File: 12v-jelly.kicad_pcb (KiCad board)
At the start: 4 copper layers, 46 x 68 mm, 28 parts, among them J1 PWR, J10 8, J3 1, J4 2, J5 3, J6 4, J7 5, J8 6, J9 7, SW2 SW_Push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

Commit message: MOSFET
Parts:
- added Q1: Q_NMOS_GDS, Package_TO_SOT_SMD:TO-252-3_TabPin2, F.Cu at (80.2, 24.8)
- added R4: 10k, Resistor_SMD:R_0603_1608Metric, F.Cu at (90.8, 26.2)
- moved U3 5.05 mm to (80.0, 44.8)
- moved U1 4.25 mm to (80.0, 66.2)
- moved C1 4.25 mm to (86.0, 68.0)
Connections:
- C1 pad 1: +5V -> LED_PWR
- J10 pad 3: +5V -> LED_PWR
- J3 pad 3: +5V -> LED_PWR
- J4 pad 3: +5V -> LED_PWR
- J5 pad 3: +5V -> LED_PWR
- J6 pad 3: +5V -> LED_PWR
- J7 pad 3: +5V -> LED_PWR
- J8 pad 3: +5V -> LED_PWR
- J9 pad 3: +5V -> LED_PWR
- U1 pad 10: +5V -> LED_PWR
- U1 pad 16: +5V -> LED_PWR
- U2 pad 2: unconnected-(U2-GPIO1-Pad2) -> /LED_EN
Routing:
- net +5V: track 26.1 -> 83.4 mm, vias 2 -> 1
- net LED_PWR: track 0.00 -> 13.7 mm, vias 0 -> 9
- net /LED_EN: track 0.00 -> 7.15 mm, vias 0 -> 1
- net Net-(J4-Pin_2): track 32.9 -> 37.2 mm
- net Net-(J10-Pin_2): track 40.9 -> 45.2 mm
- net Net-(J9-Pin_2): track 31.8 -> 36.1 mm
- net Net-(J8-Pin_2): track 32.5 -> 36.8 mm
- net Net-(J6-Pin_2): track 43.6 -> 47.9 mm
- net Net-(J5-Pin_2): track 33.5 -> 37.7 mm
- net Net-(J7-Pin_2): track 43.3 -> 47.6 mm
- net Net-(J3-Pin_2): track 47.6 -> 51.9 mm
- net /CLOCK: track 11.8 -> 9.67 mm
- net /DATA: track 26.3 -> 28.1 mm
- net /LATCH: track 11.3 -> 13.0 mm
- net Net-(J1-Pin_2): track 22.9 -> 21.2 mm
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- added copper zone on F.Cu, net +5V
- added copper zone on F.Cu, net LED_PWR
- added copper zone on In1.Cu, net LED_PWR
- removed copper zone on In1.Cu, net +5V
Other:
- board text added: "12v Jelly Eve Bytheway 24-04-01"

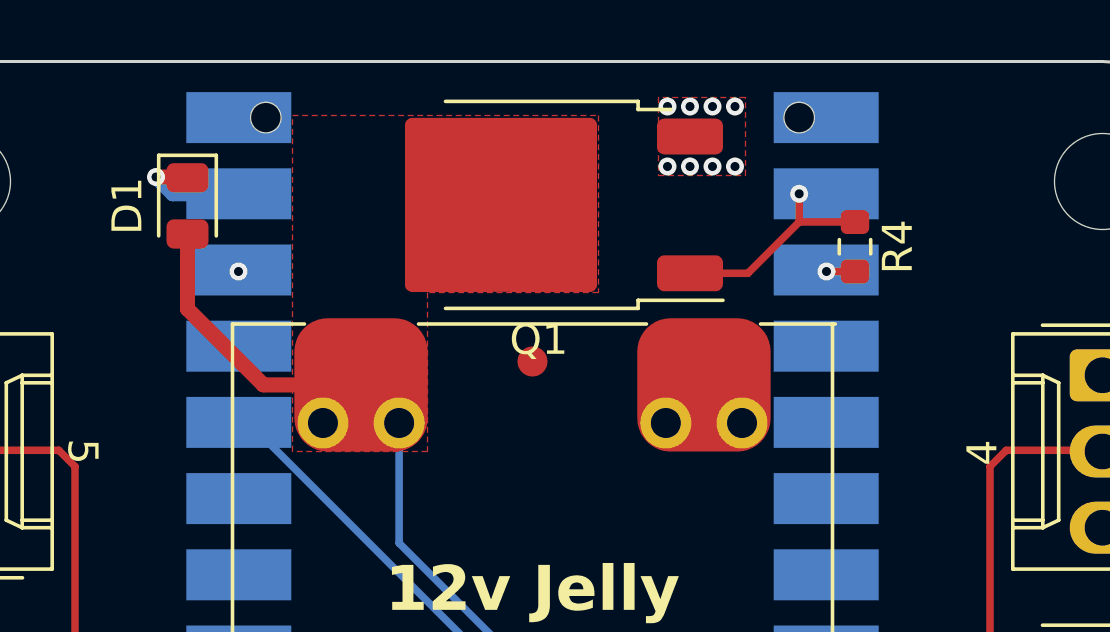
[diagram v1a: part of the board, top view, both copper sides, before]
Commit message: PMOS not NMOS
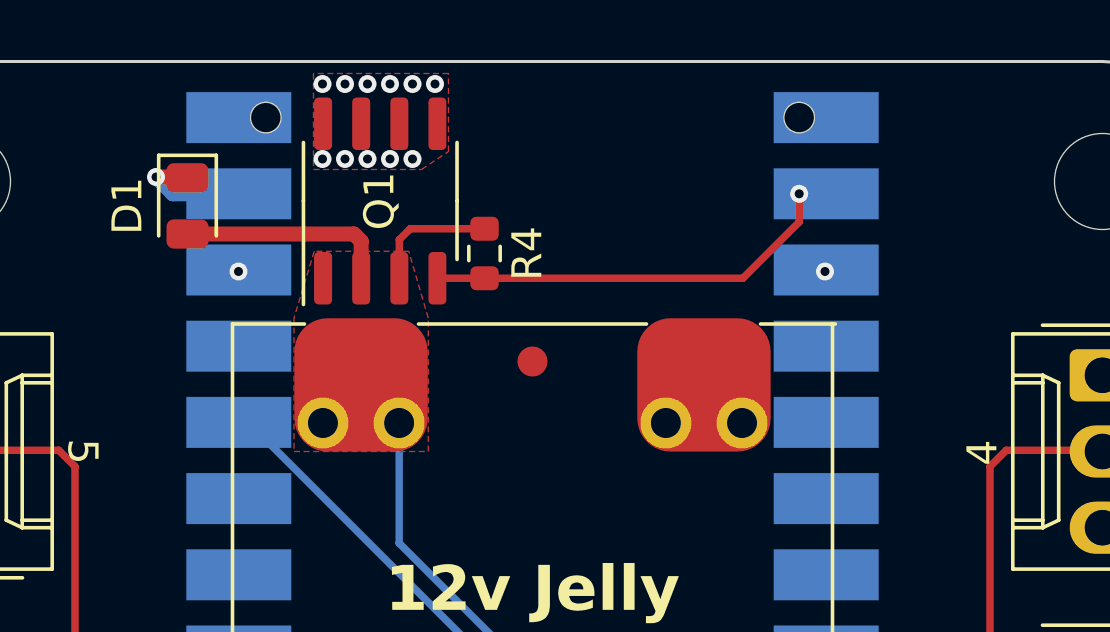
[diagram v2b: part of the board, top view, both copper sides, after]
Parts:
- Q1: value Q_NMOS_GDS -> DMP2022LSS-13; footprint Package_TO_SOT_SMD:TO-252-3_TabPin2 -> Package_SO:SO-8_3.9x4.9mm_P1.27mm
- moved R4 12.4 mm to (78.4, 26.4)
- moved Q1 5.29 mm to (74.9, 24.6), turned to 90 degrees
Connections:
- Q1 pad 1: /LED_EN -> +5V
- Q1 pad 3: LED_PWR -> +5V
- R4 pad 1: /LED_EN -> +5V
- R4 pad 2: GND -> /LED_EN
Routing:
- net /LED_EN: track 7.15 -> 13.8 mm
- net +5V: track 83.4 -> 85.4 mm
- net GND: track 15.3 -> 14.4 mm
- net LED_PWR: vias 9 -> 12
